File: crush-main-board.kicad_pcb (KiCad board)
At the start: 2 copper layers, 1 part, among them U1 Teensy4.1

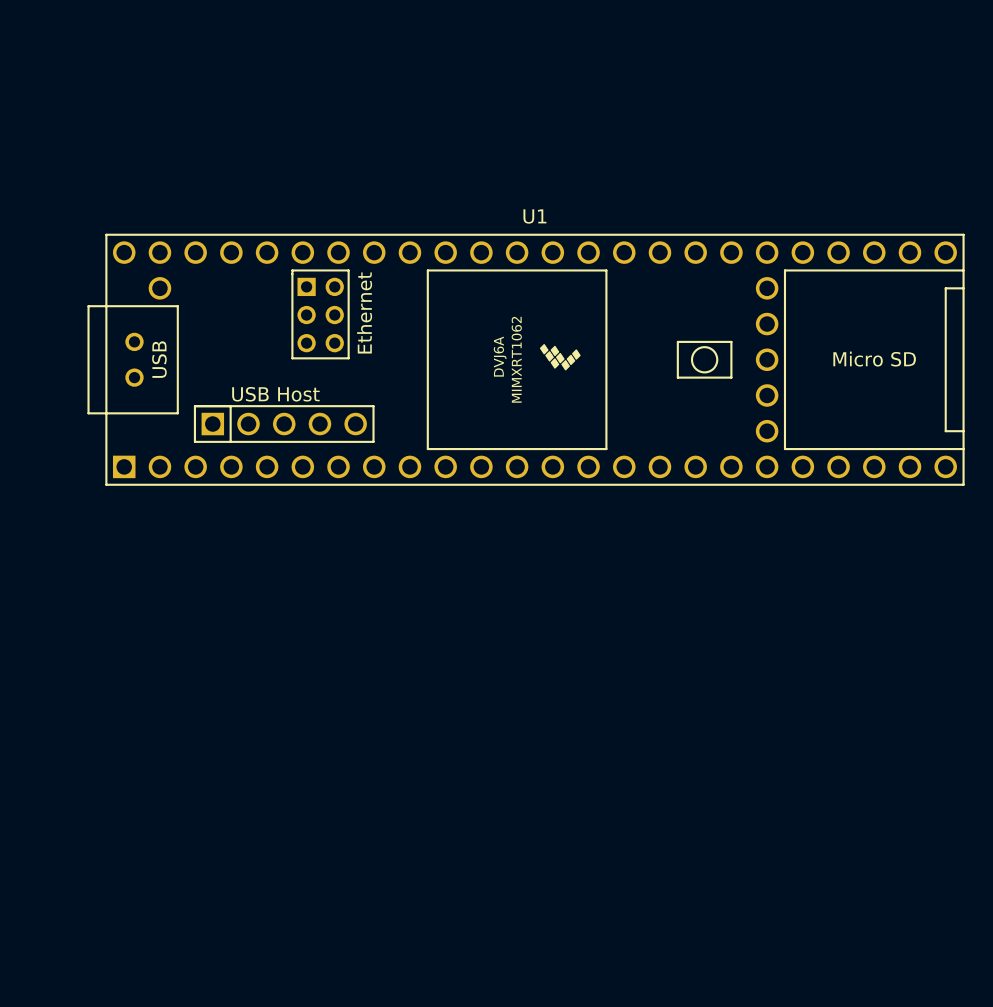
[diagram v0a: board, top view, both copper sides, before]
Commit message: Deleted some unnecessary files that were renamed
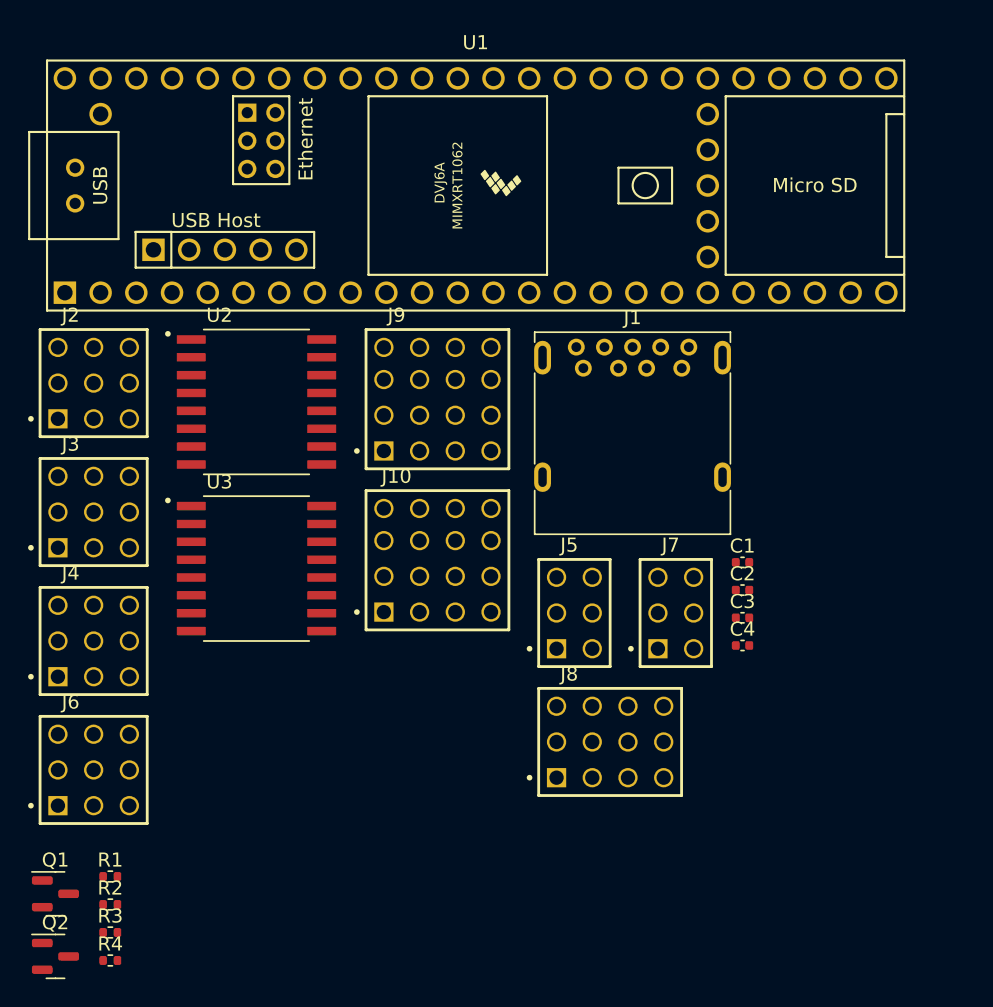
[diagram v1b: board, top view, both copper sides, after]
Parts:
- added C1: 0.1 uF, Capacitor_SMD:C_0402_1005Metric, F.Cu at (195.1, 93.2)
- added C2: 0.1 uF, Capacitor_SMD:C_0402_1005Metric, F.Cu at (195.1, 95.1)
- added C3: 0.1 uF, Capacitor_SMD:C_0402_1005Metric, F.Cu at (195.1, 97.1)
- added C4: 0.1 uF, Capacitor_SMD:C_0402_1005Metric, F.Cu at (195.1, 99.1)
- added J1: USB_B_Micro, Connector_USB:USB3_A_Molex_48393-001, F.Cu at (183.8, 79.3)
- added J10: 4x4_Header, Crush_Mainboard_Footprints:4x4_Header, F.Cu at (173.4, 92.9)
- added J2: 3x3 Header, Crush_Mainboard_Footprints:3x3_Header, F.Cu at (149.0, 80.4)
- added J3: 3x3 Header, Crush_Mainboard_Footprints:3x3_Header, F.Cu at (149.0, 89.6)
- added J4: 3x3 Header, Crush_Mainboard_Footprints:3x3_Header, F.Cu at (149.0, 98.7)
- added J5: 3x2 Header, Crush_Mainboard_Footprints:3x2_Header, F.Cu at (183.1, 96.8)
- added J6: 3x3 Header, Crush_Mainboard_Footprints:3x3_Header, F.Cu at (149.0, 107.9)
- added J7: 3x2 Header, Crush_Mainboard_Footprints:3x2_Header, F.Cu at (190.4, 96.8)
- added J8: 3x4_Header, Crush_Mainboard_Footprints:3x4_Header, F.Cu at (185.7, 105.9)
- added J9: 4x4_Header, Crush_Mainboard_Footprints:4x4_Header, F.Cu at (173.4, 81.4)
- added Q1: BSN20, Package_TO_SOT_SMD:SOT-23, F.Cu at (146.2, 116.7)
- added Q2: BSN20, Package_TO_SOT_SMD:SOT-23, F.Cu at (146.2, 121.2)
- added R1: 4K7, Resistor_SMD:R_0402_1005Metric, F.Cu at (150.1, 115.5)
- added R2: 4K7, Resistor_SMD:R_0402_1005Metric, F.Cu at (150.1, 117.5)
- added R3: 4K7, Resistor_SMD:R_0402_1005Metric, F.Cu at (150.1, 119.5)
- added R4: 4K7, Resistor_SMD:R_0402_1005Metric, F.Cu at (150.1, 121.5)
- added U2: ISO7740DW, Crush_Mainboard_Footprints:SOIC127P1030X265-16N, F.Cu at (160.5, 81.7)
- added U3: ISO7740DW, Crush_Mainboard_Footprints:SOIC127P1030X265-16N, F.Cu at (160.5, 93.6)
- U1: footprint Teensy:Teensy41 -> Crush_Mainboard_Footprints:Teensy41
- moved U1 13.1 mm to (176.1, 66.3)
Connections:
- U1 pad 1: unconnected-(U1-Pad1) -> GND
- U1 pad 10: unconnected-(U1-Pad10) -> PWM8
- U1 pad 11: unconnected-(U1-Pad11) -> PWM9
- U1 pad 13: unconnected-(U1-Pad13) -> SPI_SDO
- U1 pad 14: unconnected-(U1-Pad14) -> SPI_SDI
- U1 pad 16: unconnected-(U1-Pad16) -> PWM24
- U1 pad 17: unconnected-(U1-Pad17) -> PWM25
- U1 pad 19: unconnected-(U1-Pad19) -> Kill
- U1 pad 2: unconnected-(U1-Pad2) -> UART_RX
- U1 pad 20: unconnected-(U1-Pad20) -> PWM28
- U1 pad 21: unconnected-(U1-Pad21) -> PWM29
- U1 pad 22: unconnected-(U1-Pad22) -> DIO30
- U1 pad 23: unconnected-(U1-Pad23) -> DIO31
- U1 pad 24: unconnected-(U1-Pad24) -> DIO32
- U1 pad 25: unconnected-(U1-Pad25) -> PWM33
- U1 pad 26: unconnected-(U1-Pad26) -> DIO34
- U1 pad 27: unconnected-(U1-Pad27) -> DIO35
- U1 pad 28: unconnected-(U1-Pad28) -> PWM36
- U1 pad 29: unconnected-(U1-Pad29) -> PWM37
- U1 pad 3: unconnected-(U1-Pad3) -> UART_TX
- U1 pad 30: unconnected-(U1-Pad30) -> A/DIO38
- U1 pad 31: unconnected-(U1-Pad31) -> A/DIO39
- U1 pad 32: unconnected-(U1-Pad32) -> A/DIO40
- U1 pad 33: unconnected-(U1-Pad33) -> A/DIO41
- U1 pad 34: unconnected-(U1-Pad34) -> GND
- U1 pad 35: unconnected-(U1-Pad35) -> SPI_SCK
- U1 pad 36: unconnected-(U1-Pad36) -> PWM14
- U1 pad 37: unconnected-(U1-Pad37) -> PWM15
- U1 pad 38: unconnected-(U1-Pad38) -> A/DIO16
- U1 pad 39: unconnected-(U1-Pad39) -> A/DIO17
- U1 pad 4: unconnected-(U1-Pad4) -> PWM2
- U1 pad 40: unconnected-(U1-Pad40) -> SDA_3V3
- U1 pad 41: unconnected-(U1-Pad41) -> SCL_3V3
- U1 pad 42: unconnected-(U1-Pad42) -> A/DIO20
- U1 pad 43: unconnected-(U1-Pad43) -> A/DIO21
- U1 pad 44: unconnected-(U1-Pad44) -> PWM22
- U1 pad 45: unconnected-(U1-Pad45) -> PWM23
- U1 pad 47: unconnected-(U1-Pad47) -> GND
- U1 pad 48: unconnected-(U1-Pad48) -> +5V
- U1 pad 5: unconnected-(U1-Pad5) -> PWM3
- U1 pad 55: unconnected-(U1-Pad55) -> USB_5V
- U1 pad 56: unconnected-(U1-Pad56) -> USB_D-
- U1 pad 57: unconnected-(U1-Pad57) -> USB_D+
- U1 pad 58: unconnected-(U1-Pad58) -> GND
- U1 pad 59: unconnected-(U1-Pad59) -> GND
- U1 pad 6: unconnected-(U1-Pad6) -> PWM4
- U1 pad 7: unconnected-(U1-Pad7) -> PWM5
- U1 pad 8: unconnected-(U1-Pad8) -> PWM6
- U1 pad 9: unconnected-(U1-Pad9) -> PWM7

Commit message: Add SPI, UART, ESC Headers; Fixed library stuff
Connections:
- J10 pad 02: GND -> SDA_5V
- J10 pad 04: +5V -> GND
- J10 pad 05: GND -> +5V
- J10 pad 06: SCL_5V -> SDA_5V
- J10 pad 07: +5V -> SCL_5V
- J10 pad 09: SCL_5V -> +5V
- J10 pad 10: +5V -> SDA_5V
- J10 pad 11: GND -> SCL_5V
- J10 pad 12: SCL_5V -> GND
- J10 pad 13: (no net) -> +5V
- J10 pad 14: (no net) -> SDA_5V
- J10 pad 15: (no net) -> SCL_5V
- J10 pad 16: (no net) -> GND
- J9 pad 02: GND -> SDA_3V3
- J9 pad 04: +5V -> GND
- J9 pad 05: GND -> +5V
- J9 pad 06: SCL_3V3 -> SDA_3V3
- J9 pad 07: +5V -> SCL_3V3
- J9 pad 09: SCL_3V3 -> +5V
- J9 pad 10: +5V -> SDA_3V3
- J9 pad 11: GND -> SCL_3V3
- J9 pad 12: SCL_3V3 -> GND
- J9 pad 13: (no net) -> +5V
- J9 pad 14: (no net) -> SDA_3V3
- J9 pad 15: (no net) -> SCL_3V3
- J9 pad 16: (no net) -> GND
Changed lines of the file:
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@@
       (net 9 "+5V") (pinfunction "01") (pintype "passive"))
     (pad "02" thru_hole circle (at -3.81 1.27) (size 1.37 1.37) (drill 1.02) (layers "*.Cu" "*.Mask")
-      (net 1 "GND") (pinfunction "02") (pintype "passive"))
+      (net 31 "SDA_3V3") (pinfunction "02") (pintype "passive"))
     (pad "03" thru_hole circle (at -3.81 -1.27) (size 1.37 1.37) (drill 1.02) (layers "*.Cu" "*.Mask")
       (net 29 "SCL_3V3") (pinfunction "03") (pintype "passive"))
     (pad "04" thru_hole circle (at -3.81 -3.556) (size 1.37 1.37) (drill 1.02) (layers "*.Cu" "*.Mask")
-      (net 9 "+5V") (pinfunction "04") (pintype "passive"))
+      (net 1 "GND") (pinfunction "04") (pintype "passive"))
     (pad "05" thru_hole circle (at -1.27 3.81) (size 1.37 1.37) (drill 1.02) (layers "*.Cu" "*.Mask")
-      (net 1 "GND") (pinfunction "05") (pintype "passive"))
+      (net 9 "+5V") (pinfunction "05") (pintype "passive"))
     (pad "06" thru_hole circle (at -1.27 1.27) (size 1.37 1.37) (drill 1.02) (layers "*.Cu" "*.Mask")
-      (net 29 "SCL_3V3") (pinfunction "06") (pintype "passive"))
+      (net 31 "SDA_3V3") (pinfunction "06") (pintype "passive"))
     (pad "07" thru_hole circle (at -1.27 -1.27) (size 1.37 1.37) (drill 1.02) (layers "*.Cu" "*.Mask")
-      (net 9 "+5V") (pinfunction "07") (pintype "passive"))
+      (net 29 "SCL_3V3") (pinfunction "07") (pintype "passive"))
     (pad "08" thru_hole circle (at -1.27 -3.556) (size 1.37 1.37) (drill 1.02) (layers "*.Cu" "*.Mask")
       (net 1 "GND") (pinfunction "08") (pintype "passive"))
     (pad "09" thru_hole circle (at 1.27 3.81) (size 1.37 1.37) (drill 1.02) (layers "*.Cu" "*.Mask")
-      (net 29 "SCL_3V3") (pinfunction "09") (pintype "passive"))
+      (net 9 "+5V") (pinfunction "09") (pintype "passive"))
     (pad "10" thru_hole circle (at 1.27 1.27) (size 1.37 1.37) (drill 1.02) (layers "*.Cu" "*.Mask")
-      (net 9 "+5V") (pinfunction "10") (pintype "passive"))
+      (net 31 "SDA_3V3") (pinfunction "10") (pintype "passive"))
     (pad "11" thru_hole circle (at 1.27 -1.27) (size 1.37 1.37) (drill 1.02) (layers "*.Cu" "*.Mask")
-      (net 1 "GND") (pinfunction "11") (pintype "passive"))
+      (net 29 "SCL_3V3") (pinfunction "11") (pintype "passive"))
     (pad "12" thru_hole circle (at 1.27 -3.556) (size 1.37 1.37) (drill 1.02) (layers "*.Cu" "*.Mask")
-      (net 29 "SCL_3V3") (pinfunction "12") (pintype "passive"))
-    (pad "13" thru_hole circle (at 3.81 3.81) (size 1.37 1.37) (drill 1.02) (layers "*.Cu" "*.Mask"))
-    (pad "14" thru_hole circle (at 3.81 1.27) (size 1.37 1.37) (drill 1.02) (layers "*.Cu" "*.Mask"))
-    (pad "15" thru_hole circle (at 3.81 -1.27) (size 1.37 1.37) (drill 1.02) (layers "*.Cu" "*.Mask"))
-    (pad "16" thru_hole circle (at 3.81 -3.556) (size 1.37 1.37) (drill 1.02) (layers "*.Cu" "*.Mask"))
+      (net 1 "GND") (pinfunction "12") (pintype "passive"))
+    (pad "13" thru_hole circle (at 3.81 3.81) (size 1.37 1.37) (drill 1.02) (layers "*.Cu" "*.Mask")
+      (net 9 "+5V") (pinfunction "13") (pintype "passive"))
+    (pad "14" thru_hole circle (at 3.81 1.27) (size 1.37 1.37) (drill 1.02) (layers "*.Cu" "*.Mask")
+      (net 31 "SDA_3V3") (pinfunction "14") (pintype "passive"))
+    (pad "15" thru_hole circle (at 3.81 -1.27) (size 1.37 1.37) (drill 1.02) (layers "*.Cu" "*.Mask")
+      (net 29 "SCL_3V3") (pinfunction "15") (pintype "passive"))
+    (pad "16" thru_hole circle (at 3.81 -3.556) (size 1.37 1.37) (drill 1.02) (layers "*.Cu" "*.Mask")
+      (net 1 "GND") (pinfunction "16") (pintype "passive"))
   )
   (footprint "Resistor_SMD:R_0402_1005Metric" (layer "F.Cu")
@@
       (net 9 "+5V") (pinfunction "01") (pintype "passive"))
     (pad "02" thru_hole circle (at -3.81 1.27) (size 1.37 1.37) (drill 1.02) (layers "*.Cu" "*.Mask")
-      (net 1 "GND") (pinfunction "02") (pintype "passive"))
+      (net 32 "SDA_5V") (pinfunction "02") (pintype "passive"))
     (pad "03" thru_hole circle (at -3.81 -1.27) (size 1.37 1.37) (drill 1.02) (layers "*.Cu" "*.Mask")
       (net 30 "SCL_5V") (pinfunction "03") (pintype "passive"))
     (pad "04" thru_hole circle (at -3.81 -3.556) (size 1.37 1.37) (drill 1.02) (layers "*.Cu" "*.Mask")
-      (net 9 "+5V") (pinfunction "04") (pintype "passive"))
+      (net 1 "GND") (pinfunction "04") (pintype "passive"))
     (pad "05" thru_hole circle (at -1.27 3.81) (size 1.37 1.37) (drill 1.02) (layers "*.Cu" "*.Mask")
-      (net 1 "GND") (pinfunction "05") (pintype "passive"))
+      (net 9 "+5V") (pinfunction "05") (pintype "passive"))
     (pad "06" thru_hole circle (at -1.27 1.27) (size 1.37 1.37) (drill 1.02) (layers "*.Cu" "*.Mask")
-      (net 30 "SCL_5V") (pinfunction "06") (pintype "passive"))
+      (net 32 "SDA_5V") (pinfunction "06") (pintype "passive"))
     (pad "07" thru_hole circle (at -1.27 -1.27) (size 1.37 1.37) (drill 1.02) (layers "*.Cu" "*.Mask")
-      (net 9 "+5V") (pinfunction "07") (pintype "passive"))
+      (net 30 "SCL_5V") (pinfunction "07") (pintype "passive"))
     (pad "08" thru_hole circle (at -1.27 -3.556) (size 1.37 1.37) (drill 1.02) (layers "*.Cu" "*.Mask")
       (net 1 "GND") (pinfunction "08") (pintype "passive"))
     (pad "09" thru_hole circle (at 1.27 3.81) (size 1.37 1.37) (drill 1.02) (layers "*.Cu" "*.Mask")
-      (net 30 "SCL_5V") (pinfunction "09") (pintype "passive"))
+      (net 9 "+5V") (pinfunction "09") (pintype "passive"))
     (pad "10" thru_hole circle (at 1.27 1.27) (size 1.37 1.37) (drill 1.02) (layers "*.Cu" "*.Mask")
-      (net 9 "+5V") (pinfunction "10") (pintype "passive"))
+      (net 32 "SDA_5V") (pinfunction "10") (pintype "passive"))
     (pad "11" thru_hole circle (at 1.27 -1.27) (size 1.37 1.37) (drill 1.02) (layers "*.Cu" "*.Mask")
-      (net 1 "GND") (pinfunction "11") (pintype "passive"))
+      (net 30 "SCL_5V") (pinfunction "11") (pintype "passive"))
     (pad "12" thru_hole circle (at 1.27 -3.556) (size 1.37 1.37) (drill 1.02) (layers "*.Cu" "*.Mask")
-      (net 30 "SCL_5V") (pinfunction "12") (pintype "passive"))
-    (pad "13" thru_hole circle (at 3.81 3.81) (size 1.37 1.37) (drill 1.02) (layers "*.Cu" "*.Mask"))
-    (pad "14" thru_hole circle (at 3.81 1.27) (size 1.37 1.37) (drill 1.02) (layers "*.Cu" "*.Mask"))
-    (pad "15" thru_hole circle (at 3.81 -1.27) (size 1.37 1.37) (drill 1.02) (layers "*.Cu" "*.Mask"))
-    (pad "16" thru_hole circle (at 3.81 -3.556) (size 1.37 1.37) (drill 1.02) (layers "*.Cu" "*.Mask"))
+      (net 1 "GND") (pinfunction "12") (pintype "passive"))
+    (pad "13" thru_hole circle (at 3.81 3.81) (size 1.37 1.37) (drill 1.02) (layers "*.Cu" "*.Mask")
+      (net 9 "+5V") (pinfunction "13") (pintype "passive"))
+    (pad "14" thru_hole circle (at 3.81 1.27) (size 1.37 1.37) (drill 1.02) (layers "*.Cu" "*.Mask")
+      (net 32 "SDA_5V") (pinfunction "14") (pintype "passive"))
+    (pad "15" thru_hole circle (at 3.81 -1.27) (size 1.37 1.37) (drill 1.02) (layers "*.Cu" "*.Mask")
+      (net 30 "SCL_5V") (pinfunction "15") (pintype "passive"))
+    (pad "16" thru_hole circle (at 3.81 -3.556) (size 1.37 1.37) (drill 1.02) (layers "*.Cu" "*.Mask")
+      (net 1 "GND") (pinfunction "16") (pintype "passive"))
   )
   (footprint "Crush_Mainboard_Footprints:SOIC127P1030X265-16N" (layer "F.Cu")

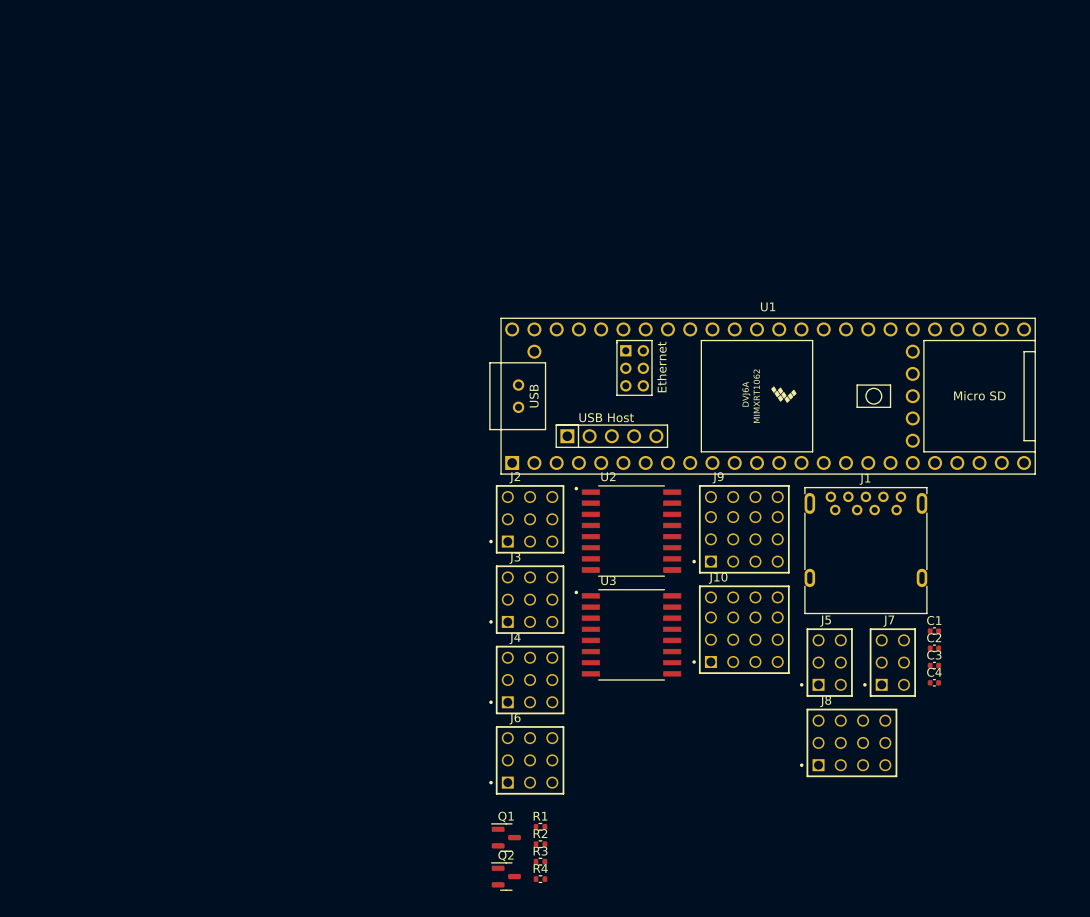
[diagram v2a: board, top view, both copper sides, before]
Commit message: Cleaned up the schematic layout & separated the footprints into corresponding groups
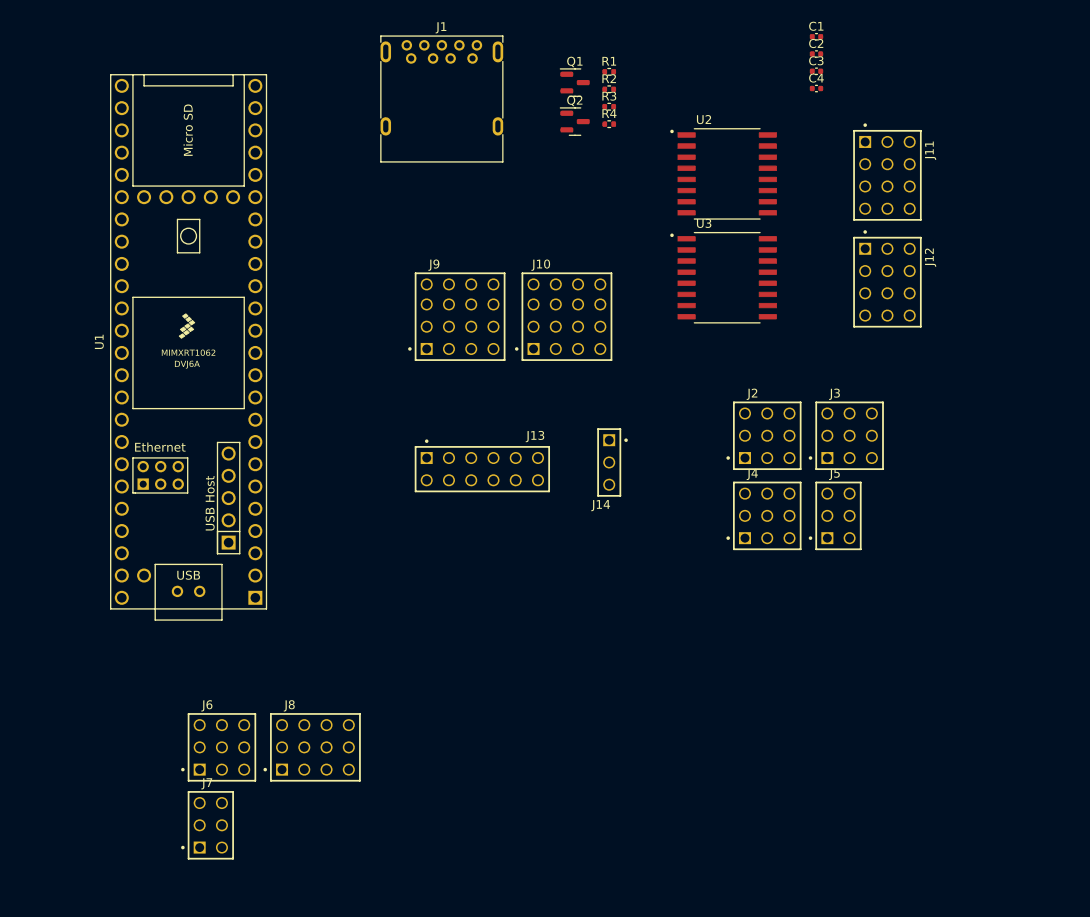
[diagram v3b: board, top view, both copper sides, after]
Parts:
- added J11: 3x4_Header, Crush_Mainboard_Footprints:3x4_Header, F.Cu at (189.7, 41.1)
- added J12: 3x4_Header, Crush_Mainboard_Footprints:3x4_Header, F.Cu at (189.7, 53.3)
- added J13: 6x2_Header, Crush_Mainboard_Footprints:6x2_Header, F.Cu at (143.5, 74.7)
- added J14: 3x1_Header, Crush_Mainboard_Footprints:3x1_Header, F.Cu at (158.0, 73.9)
- moved Q1 86.5 mm to (154.1, 30.6)
- moved Q2 86.5 mm to (154.1, 35.0)
- moved R1 86.5 mm to (158.0, 29.3)
- moved R2 86.5 mm to (158.0, 31.3)
- moved R3 86.5 mm to (158.0, 33.3)
- moved R4 86.5 mm to (158.0, 35.3)
- moved J7 80.0 mm to (112.5, 115.3)
- moved J1 70.7 mm to (135.4, 27.8)
- moved C1 69.1 mm to (181.6, 25.3)
- moved C2 69.1 mm to (181.6, 27.3)
- moved C3 69.1 mm to (181.6, 29.3)
- moved C4 69.1 mm to (181.6, 31.2)
- moved U1 66.4 mm to (110.0, 60.1), turned to 90 degrees
- moved J8 61.2 mm to (124.5, 106.4)
- moved U3 42.2 mm to (171.4, 52.8)
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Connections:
- J6 pad 02: +5V -> +3V3
- J6 pad 05: +5V -> +3V3
- J6 pad 08: +5V -> +3V3
- J7 pad 02: +3V3 -> +5V
- J7 pad 05: +3V3 -> +5V
- J8 pad 02: +5V -> +3V3
- J8 pad 05: +5V -> +3V3
- J8 pad 08: +5V -> +3V3
- J8 pad 11: +5V -> +3V3
- U1 pad 12: unconnected-(U1-10_CS_MQSR-Pad12) -> SPI_CS
- U3 pad 3: PWM6 -> PWM2
- U3 pad 4: PWM7 -> PWM3
- U3 pad 5: PWM8 -> PWM4
- U3 pad 6: PWM9 -> PWM5
